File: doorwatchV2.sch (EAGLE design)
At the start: 24 parts, among them IC2 MAX3232CPE, Q1 IRLZ44Z, X2 D-SUB9-H2M09RA, X3 MKDSN1,5/4-5,08

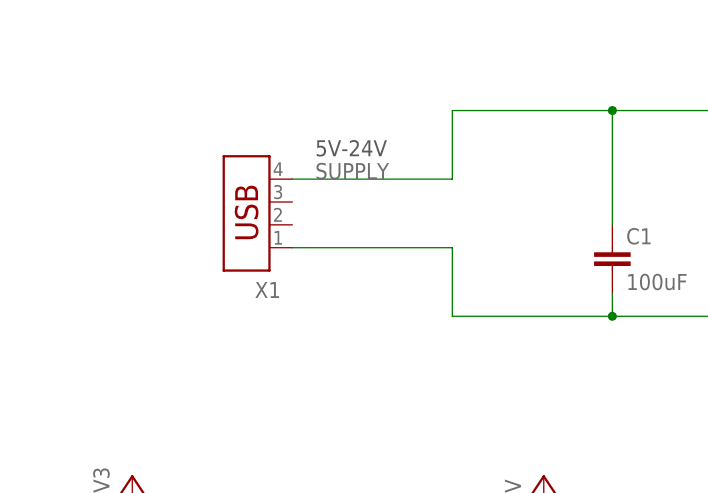
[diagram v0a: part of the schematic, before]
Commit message: changed the power plug from USB to print connector (con-conrad)
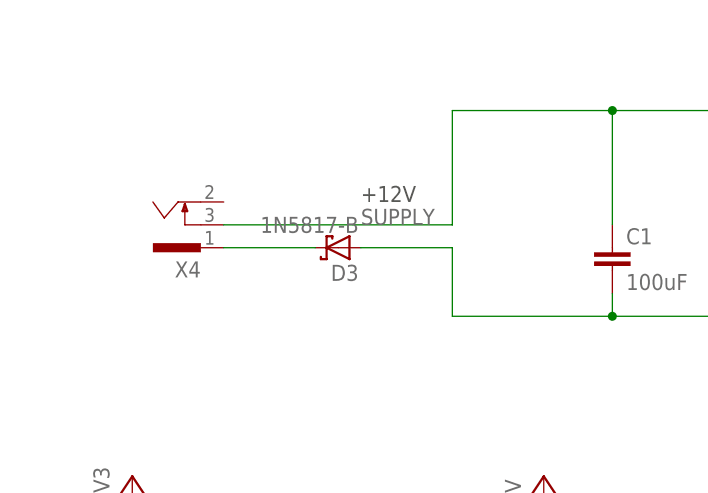
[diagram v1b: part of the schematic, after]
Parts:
- removed X1: (no value), con-amp:USB-787616
- added D3: 1N5817-B, diode:1N5817-B
- added X4: (no value), con-conrad:733980-62
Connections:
- new net N$15: D3.C, X4.1
- net GND: now also D3.A; no longer X1.1
- net SUPPLY: now also X4.3; no longer X1.4
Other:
- note added: "+12V"
- note removed: "5V-24V"
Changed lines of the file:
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@@
 <part name="C2" library="rcl" deviceset="CPOL-EU" device="E5-10.5" value="1000uF"/>
 <part name="P+1" library="supply1" deviceset="+5V" device=""/>
-<part name="X1" library="con-amp" deviceset="USB-787616" device=""/>
 <part name="SV1" library="con-harting-ml" deviceset="ML26" device=""/>
 <part name="GND2" library="supply1" deviceset="GND" device=""/>
@@
 <part name="R5" library="rcl" deviceset="R-EU_" device="M0805" value="10k"/>
 <part name="X3" library="con-phoenix-508" deviceset="MKDSN1,5/4-5,08" device=""/>
+<part name="X4" library="con-conrad" deviceset="73398?" device="0-62"/>
+<part name="D3" library="diode" deviceset="1N581*" device="" technology="7-B"/>
 </parts>
 <sheets>
 <sheet>
 <plain>
-<text x="-50.8" y="71.12" size="1.778" layer="97">5V-24V</text>
+<text x="-45.72" y="66.04" size="1.778" layer="97">+12V</text>
 </plain>
 <instances>
@@
 <instance part="C2" gate="G$1" x="63.5" y="60.96"/>
 <instance part="P+1" gate="1" x="76.2" y="83.82"/>
-<instance part="X1" gate="G$1" x="-58.42" y="66.04" rot="R180"/>
 <instance part="SV1" gate="1" x="-48.26" y="7.62" rot="R180"/>
 <instance part="GND2" gate="1" x="-25.4" y="-20.32"/>
@@
 <instance part="X3" gate="-3" x="0" y="-111.76"/>
 <instance part="X3" gate="-4" x="0" y="-116.84"/>
+<instance part="X4" gate="G$1" x="-66.04" y="63.5" rot="R180"/>
+<instance part="D3" gate="G$1" x="-48.26" y="60.96" rot="R180"/>
 </instances>
 <busses>
@@
 <wire x1="-17.78" y1="53.34" x2="-2.54" y2="53.34" width="0.1524" layer="91"/>
 <junction x="-2.54" y="53.34"/>
-<pinref part="X1" gate="G$1" pin="1"/>
-<wire x1="-53.34" y1="60.96" x2="-35.56" y2="60.96" width="0.1524" layer="91"/>
 <wire x1="-35.56" y1="60.96" x2="-35.56" y2="53.34" width="0.1524" layer="91"/>
 <wire x1="-35.56" y1="53.34" x2="-17.78" y2="53.34" width="0.1524" layer="91"/>
 <junction x="-17.78" y="53.34"/>
+<pinref part="D3" gate="G$1" pin="A"/>
+<wire x1="-45.72" y1="60.96" x2="-35.56" y2="60.96" width="0.1524" layer="91"/>
 </segment>
 <segment>
@@
 <wire x1="-17.78" y1="76.2" x2="-17.78" y2="63.5" width="0.1524" layer="91"/>
 <junction x="-17.78" y="76.2"/>
-<label x="-50.8" y="68.58" size="1.778" layer="95"/>
-<pinref part="X1" gate="G$1" pin="4"/>
-<wire x1="-53.34" y1="68.58" x2="-35.56" y2="68.58" width="0.1524" layer="91"/>
-<wire x1="-35.56" y1="68.58" x2="-35.56" y2="76.2" width="0.1524" layer="91"/>
+<label x="-45.72" y="63.5" size="1.778" layer="95"/>
+<wire x1="-35.56" y1="63.5" x2="-35.56" y2="76.2" width="0.1524" layer="91"/>
+<pinref part="X4" gate="G$1" pin="3"/>
+<wire x1="-60.96" y1="63.5" x2="-35.56" y2="63.5" width="0.1524" layer="91"/>
 </segment>
 </net>
@@
 </segment>
 </net>
+<net name="N$15" class="0">
+<segment>
+<pinref part="X4" gate="G$1" pin="1"/>
+<pinref part="D3" gate="G$1" pin="C"/>
+<wire x1="-60.96" y1="60.96" x2="-50.8" y2="60.96" width="0.1524" layer="91"/>
+</segment>
+</net>

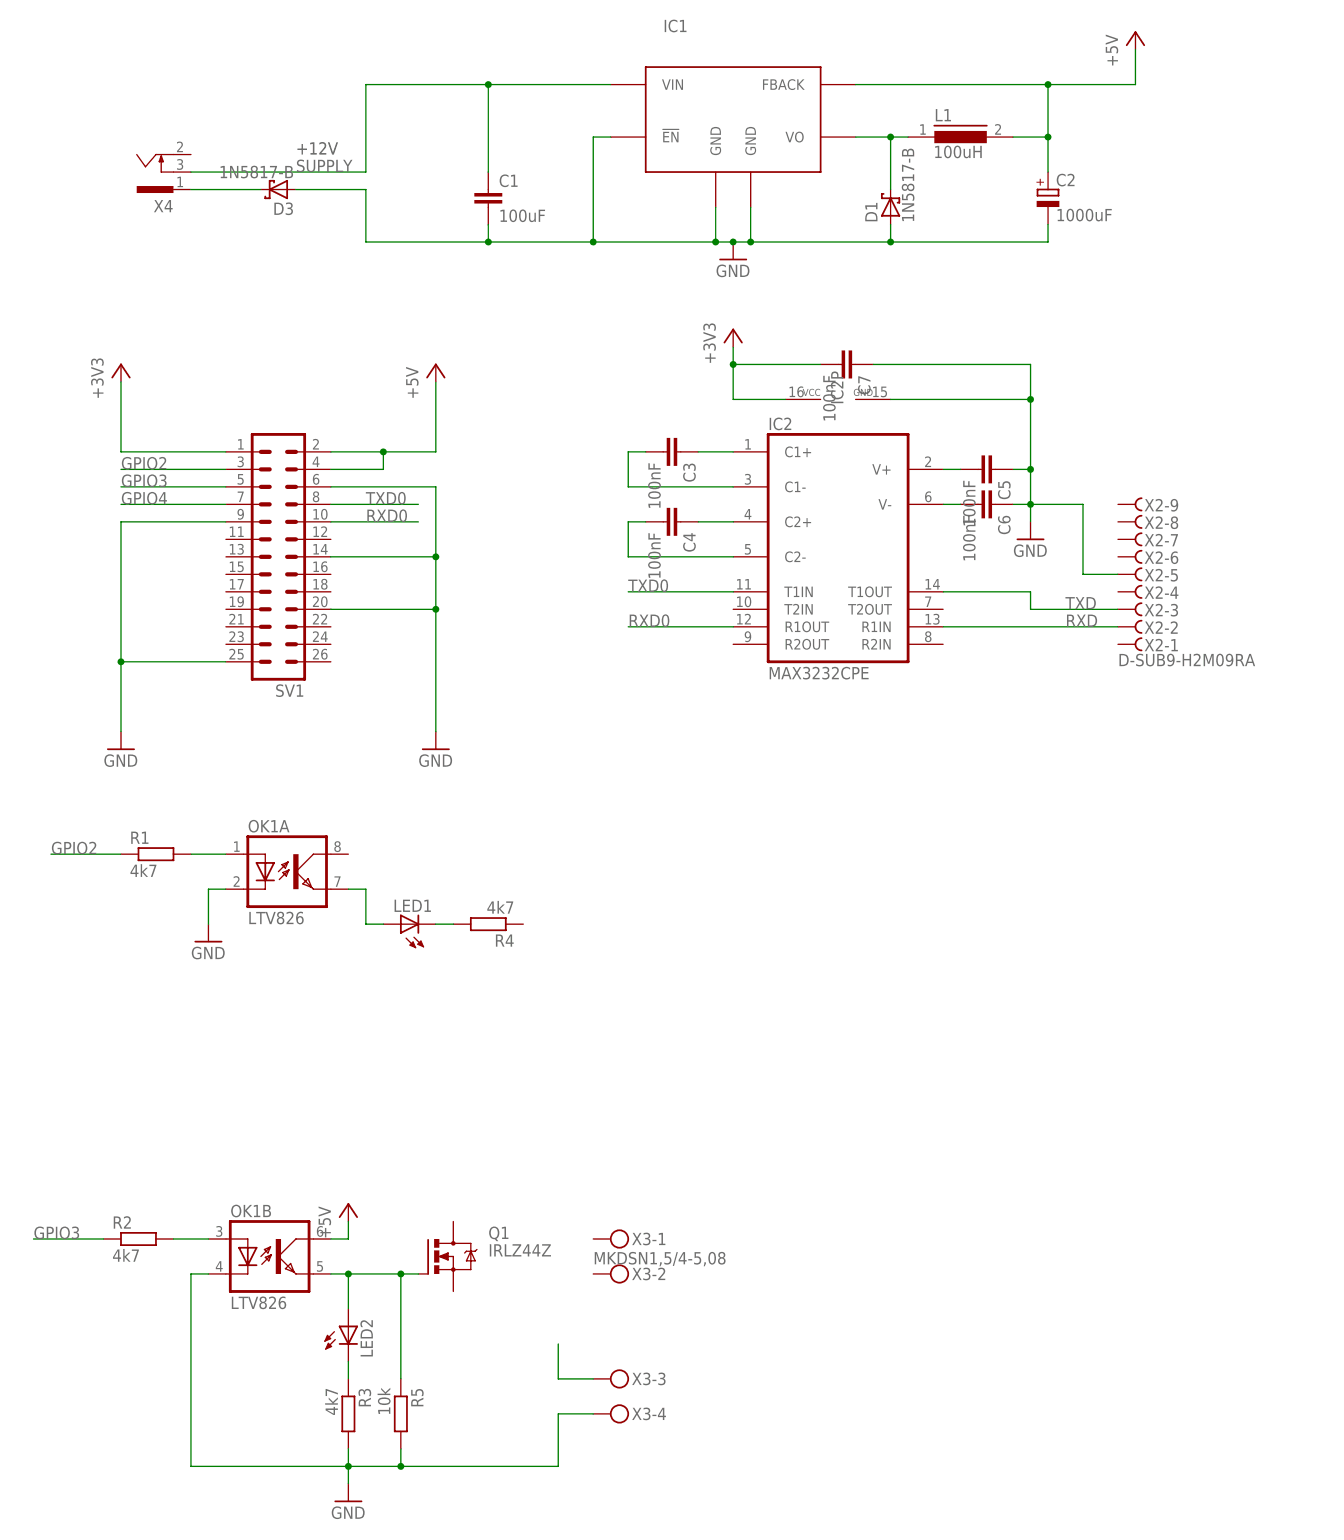
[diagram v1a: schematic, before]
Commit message: adapted the optocoupler parts to 12V supply on output.
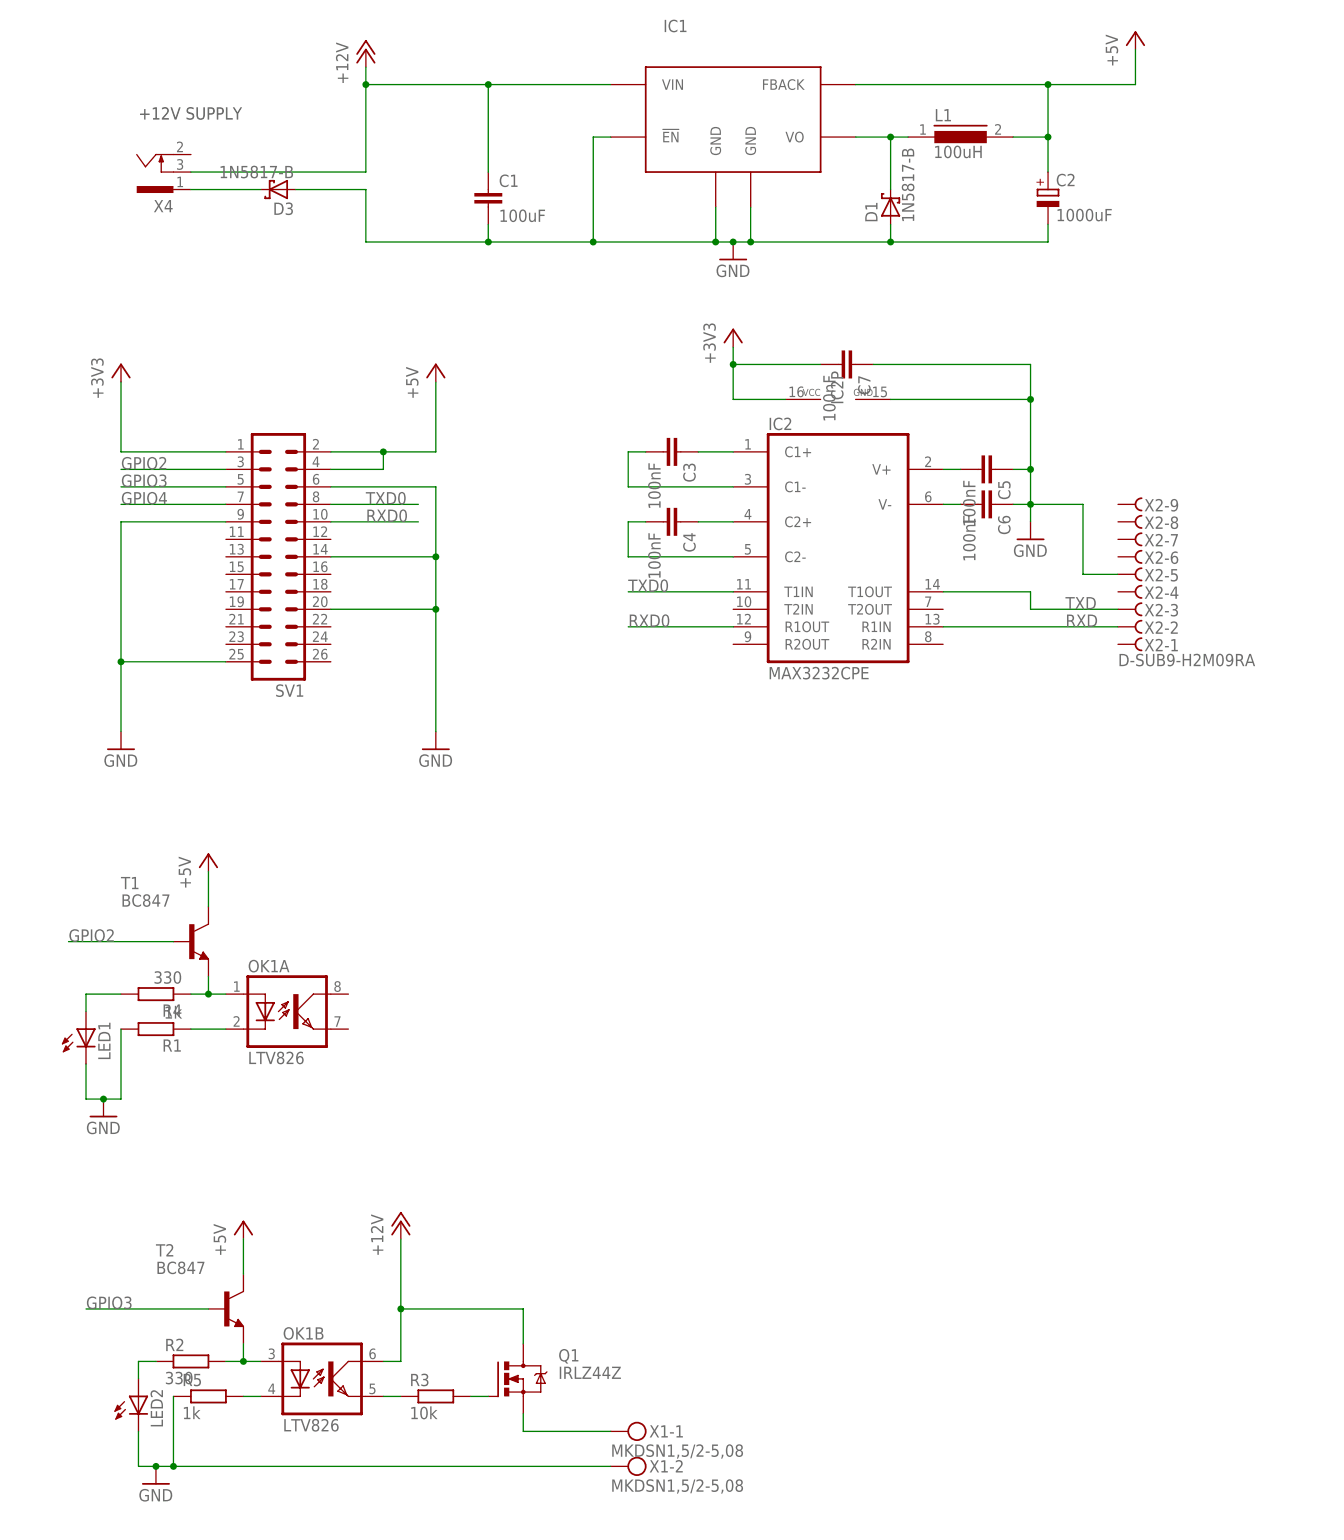
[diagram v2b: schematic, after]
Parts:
- removed X3: MKDSN1,5/4-5,08, con-phoenix-508:MKDSN1,5/4-5,08
- added T1, T2: BC847, transistor:BC847
- added X1: MKDSN1,5/2-5,08, con-phoenix-508:MKDSN1,5/2-5,08
- R1: value 4k7 -> 1k
- R2, R4: value 4k7 -> 330
- R3: value 4k7 -> 10k
- R5: value 10k -> 1k
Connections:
- removed net SUPPLY: C1.1, IC1.VIN, X4.3
- new net +12V: C1.1, IC1.VIN, OK1B.COL, Q1.D, X4.3
- new net N$16: OK1B.EMIT, R3.1
- new net N$17: Q1.G, R3.2
- net +5V: now also T1.C, T2.C; no longer OK1B.COL
- net GND: now also LED1.C, LED2.C, R1.2, R5.1, X1-2.KL; no longer OK1A.C, OK1B.C, R3.2, R5.2, X3-4.KL
- net GPIO2: now also T1.B; no longer R1.1
- net GPIO3: now also T2.B; no longer R2.1
- net N$10: now also R4.1, T1.E; no longer R1.2
- net N$11: now also OK1B.C, R5.2; no longer OK1B.A, R2.2
- net N$12: now also R4.2; no longer OK1A.EMIT
- net N$13: now also Q1.S, X1-1.KL; no longer LED2.A, OK1B.EMIT, Q1.G, R5.1
- net N$14: now also OK1A.C, R1.1; no longer LED1.C, R4.2
- net N$8: now also OK1B.A, R2.2, T2.E; no longer X3-3.KL
- net N$9: now also LED2.A, R2.1; no longer LED2.C, R3.1
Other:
- note added: "+12V SUPPLY"
- note removed: "+12V"
- moved on the sheet: LED1, LED2, OK1A, OK1B, Q1, R1, R2, R3, R4, R5

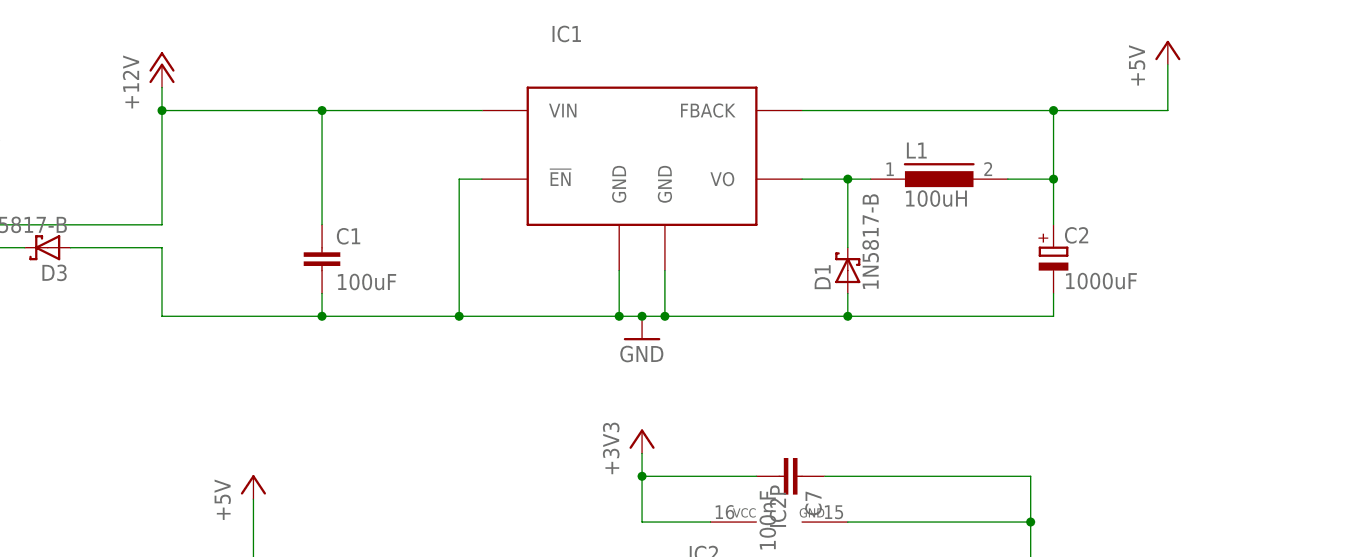
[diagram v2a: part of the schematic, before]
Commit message: added power indication LED
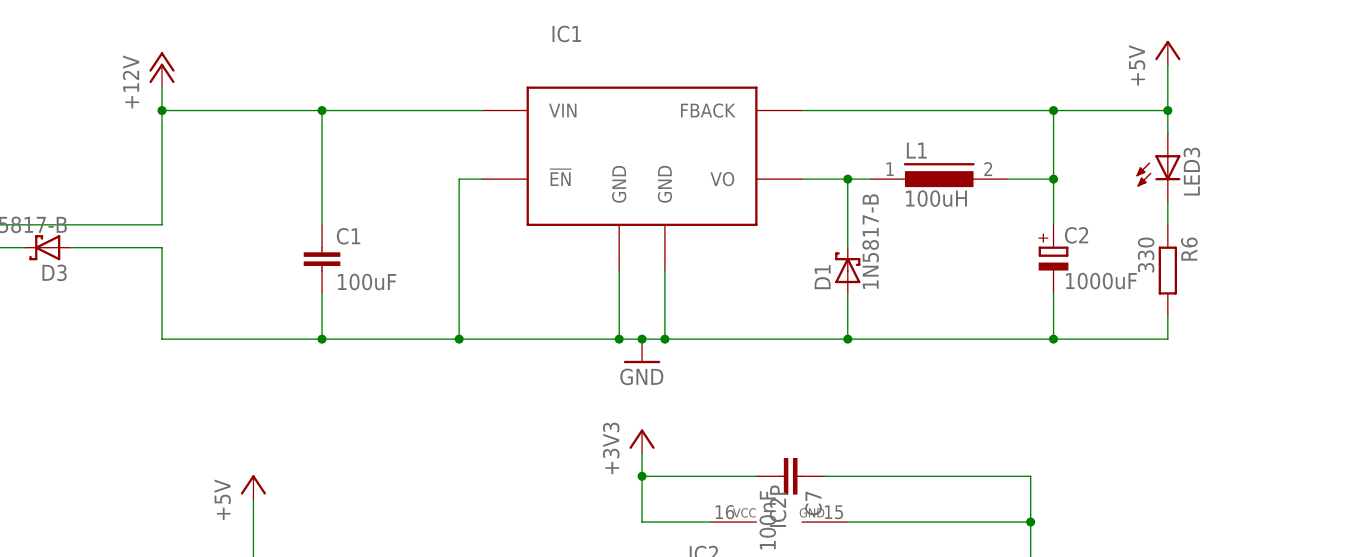
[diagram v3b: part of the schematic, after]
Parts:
- added LED3: (no value), led:LEDCHIP-LED0805
- added R6: 330, rcl:R-EU_M0805
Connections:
- new net N$18: LED3.C, R6.1
- net +5V: now also LED3.A
- net GND: now also R6.2
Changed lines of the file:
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@@
 <part name="P+6" library="supply1" deviceset="+12V" device=""/>
 <part name="X1" library="con-phoenix-508" deviceset="MKDSN1,5/2-5,08" device=""/>
+<part name="LED3" library="led" deviceset="LED" device="CHIP-LED0805"/>
+<part name="R6" library="rcl" deviceset="R-EU_" device="M0805" value="330"/>
 </parts>
 <sheets>
@@
 <instances>
 <instance part="IC1" gate="G$1" x="17.78" y="71.12"/>
-<instance part="GND1" gate="1" x="17.78" y="50.8"/>
+<instance part="GND1" gate="1" x="17.78" y="48.26"/>
 <instance part="L1" gate="G$1" x="50.8" y="68.58"/>
 <instance part="D1" gate="G$1" x="40.64" y="58.42" rot="R90"/>
@@
 <instance part="X1" gate="-1" x="2.54" y="-119.38"/>
 <instance part="X1" gate="-2" x="2.54" y="-124.46"/>
+<instance part="LED3" gate="G$1" x="76.2" y="71.12"/>
+<instance part="R6" gate="G$1" x="76.2" y="58.42" rot="R270"/>
 </instances>
 <busses>
@@
 <segment>
 <pinref part="IC1" gate="G$1" pin="GND@1"/>
-<wire x1="15.24" y1="58.42" x2="15.24" y2="53.34" width="0.1524" layer="91"/>
+<wire x1="15.24" y1="58.42" x2="15.24" y2="50.8" width="0.1524" layer="91"/>
 <pinref part="IC1" gate="G$1" pin="GND@2"/>
-<wire x1="15.24" y1="53.34" x2="17.78" y2="53.34" width="0.1524" layer="91"/>
-<wire x1="17.78" y1="53.34" x2="20.32" y2="53.34" width="0.1524" layer="91"/>
-<wire x1="20.32" y1="53.34" x2="20.32" y2="58.42" width="0.1524" layer="91"/>
+<wire x1="15.24" y1="50.8" x2="17.78" y2="50.8" width="0.1524" layer="91"/>
+<wire x1="17.78" y1="50.8" x2="20.32" y2="50.8" width="0.1524" layer="91"/>
+<wire x1="20.32" y1="50.8" x2="20.32" y2="58.42" width="0.1524" layer="91"/>
 <pinref part="GND1" gate="1" pin="GND"/>
-<junction x="17.78" y="53.34"/>
+<junction x="17.78" y="50.8"/>
 <pinref part="IC1" gate="G$1" pin="!EN"/>
 <wire x1="0" y1="68.58" x2="-2.54" y2="68.58" width="0.1524" layer="91"/>
-<wire x1="-2.54" y1="68.58" x2="-2.54" y2="53.34" width="0.1524" layer="91"/>
-<wire x1="-2.54" y1="53.34" x2="15.24" y2="53.34" width="0.1524" layer="91"/>
-<junction x="15.24" y="53.34"/>
+<wire x1="-2.54" y1="68.58" x2="-2.54" y2="50.8" width="0.1524" layer="91"/>
+<wire x1="-2.54" y1="50.8" x2="15.24" y2="50.8" width="0.1524" layer="91"/>
+<junction x="15.24" y="50.8"/>
 <pinref part="D1" gate="G$1" pin="A"/>
-<wire x1="40.64" y1="55.88" x2="40.64" y2="53.34" width="0.1524" layer="91"/>
-<wire x1="40.64" y1="53.34" x2="20.32" y2="53.34" width="0.1524" layer="91"/>
-<junction x="20.32" y="53.34"/>
-<wire x1="63.5" y1="53.34" x2="40.64" y2="53.34" width="0.1524" layer="91"/>
-<junction x="40.64" y="53.34"/>
+<wire x1="40.64" y1="55.88" x2="40.64" y2="50.8" width="0.1524" layer="91"/>
+<wire x1="40.64" y1="50.8" x2="20.32" y2="50.8" width="0.1524" layer="91"/>
+<junction x="20.32" y="50.8"/>
+<wire x1="63.5" y1="50.8" x2="40.64" y2="50.8" width="0.1524" layer="91"/>
+<junction x="40.64" y="50.8"/>
 <pinref part="C2" gate="G$1" pin="-"/>
-<wire x1="63.5" y1="53.34" x2="63.5" y2="55.88" width="0.1524" layer="91"/>
+<wire x1="63.5" y1="50.8" x2="63.5" y2="55.88" width="0.1524" layer="91"/>
 <pinref part="C1" gate="G$1" pin="2"/>
-<wire x1="-17.78" y1="55.88" x2="-17.78" y2="53.34" width="0.1524" layer="91"/>
-<wire x1="-17.78" y1="53.34" x2="-2.54" y2="53.34" width="0.1524" layer="91"/>
-<junction x="-2.54" y="53.34"/>
-<wire x1="-35.56" y1="60.96" x2="-35.56" y2="53.34" width="0.1524" layer="91"/>
-<wire x1="-35.56" y1="53.34" x2="-17.78" y2="53.34" width="0.1524" layer="91"/>
-<junction x="-17.78" y="53.34"/>
+<wire x1="-17.78" y1="55.88" x2="-17.78" y2="50.8" width="0.1524" layer="91"/>
+<wire x1="-17.78" y1="50.8" x2="-2.54" y2="50.8" width="0.1524" layer="91"/>
+<junction x="-2.54" y="50.8"/>
+<wire x1="-35.56" y1="60.96" x2="-35.56" y2="50.8" width="0.1524" layer="91"/>
+<wire x1="-35.56" y1="50.8" x2="-17.78" y2="50.8" width="0.1524" layer="91"/>
+<junction x="-17.78" y="50.8"/>
 <pinref part="D3" gate="G$1" pin="A"/>
 <wire x1="-45.72" y1="60.96" x2="-35.56" y2="60.96" width="0.1524" layer="91"/>
+<pinref part="R6" gate="G$1" pin="2"/>
+<wire x1="76.2" y1="53.34" x2="76.2" y2="50.8" width="0.1524" layer="91"/>
+<wire x1="76.2" y1="50.8" x2="63.5" y2="50.8" width="0.1524" layer="91"/>
+<junction x="63.5" y="50.8"/>
 </segment>
 <segment>
@@
 <pinref part="P+1" gate="1" pin="+5V"/>
 <wire x1="76.2" y1="76.2" x2="76.2" y2="81.28" width="0.1524" layer="91"/>
+<pinref part="LED3" gate="G$1" pin="A"/>
+<wire x1="76.2" y1="73.66" x2="76.2" y2="76.2" width="0.1524" layer="91"/>
+<junction x="76.2" y="76.2"/>
 </segment>
 <segment>
@@
 </segment>
 </net>
+<net name="N$18" class="0">
+<segment>
+<pinref part="LED3" gate="G$1" pin="C"/>
+<pinref part="R6" gate="G$1" pin="1"/>
+<wire x1="76.2" y1="66.04" x2="76.2" y2="63.5" width="0.1524" layer="91"/>
+</segment>
+</net>
